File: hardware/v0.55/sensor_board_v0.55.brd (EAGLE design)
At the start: 56.4 x 56.4 mm, 58 parts, among them J3 USB-MICROB, J6 AVR_SPI_PRG_6PTH, U1 ATMEGA328P, U10 TSL2591, U2 SHT35, U3 OPA344, U5 FT231XS, U6 ADMP401, U7 RFM69HCW, U8 MCP1703CB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

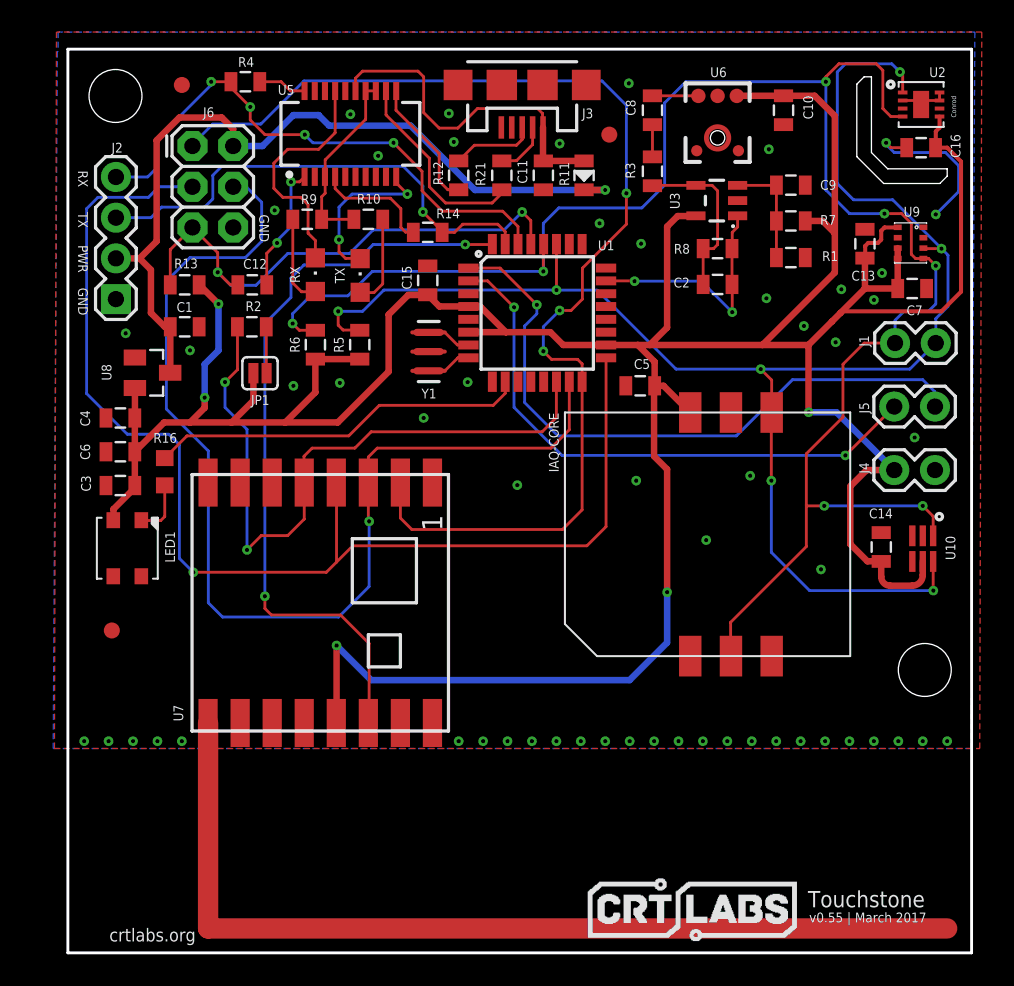
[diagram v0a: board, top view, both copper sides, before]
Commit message: v0.55 - Major design update
- Added 2x5 header for PMS7003 PM sensor
- Moved microphone+amp circuitry to accomodate for the PM sensor header
- Removed UART and software serial breakout headers
- Moved voltage regulator circuitry in space created by removing UART
header
- Moved LED in space created by moving voltage regulator
- Moved light sensor to be in line with LED
- Rerouted several traces to accomodate for new design
- Some silkscreen adjustments
- Provided some more tolerance to the mounting holes
- Moved fiducial markers
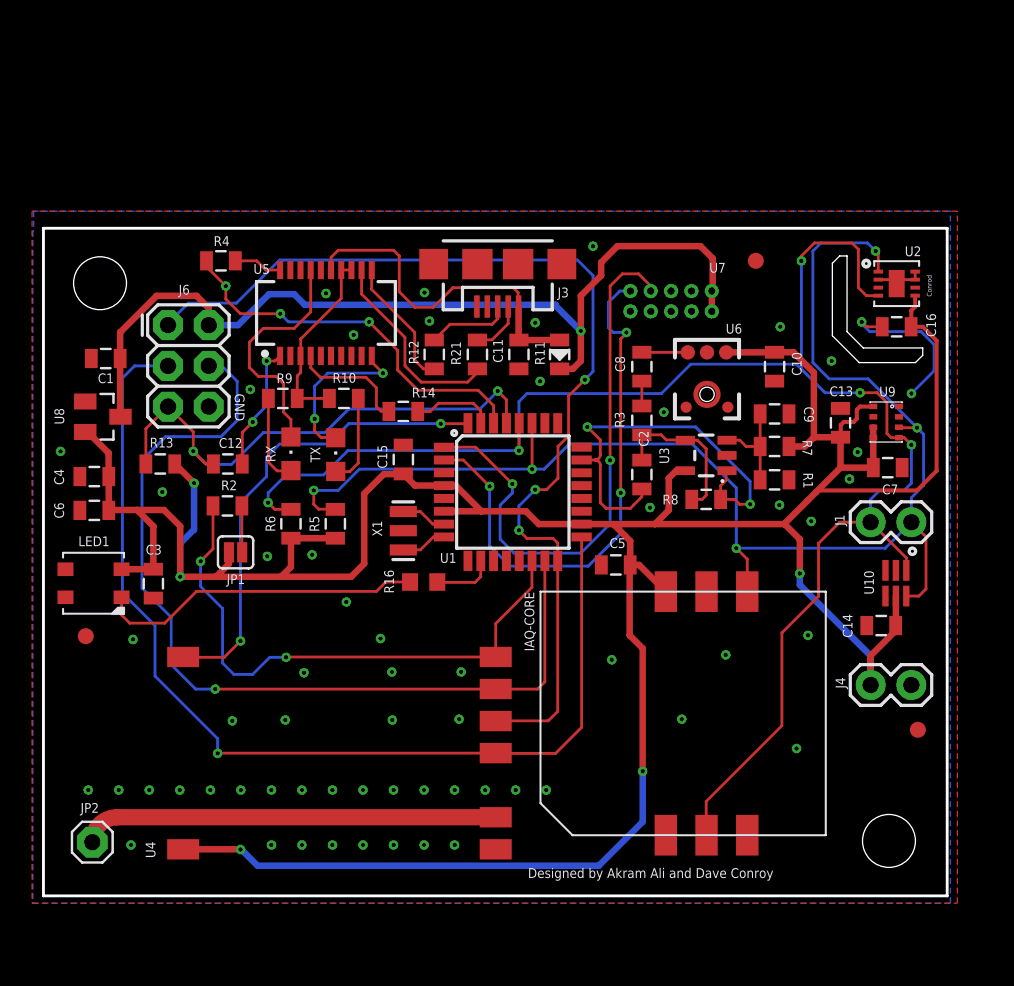
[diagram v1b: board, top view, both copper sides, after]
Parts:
- removed J2: (no value), SparkFun-Connectors:1X04
- removed J5: (no value), SparkFun-Connectors:1X02
- removed Y1: 16MHZ, SparkFun-FreqCtrl:RESONATOR-SMD
- added JP2: (no value), adafruit:1X01
- added U4: RFM69HW, RFM69 USB Gateway:LOWPOWERLAB_RFM69W-MINPADS
- added X1: 16 MHz, SparkFun:RESONATOR-SMD
- U7: value RFM69HCW -> PMS7003; device SparkFun-RF:RFM69HCW-XXXS2 -> Amphenol:RECEPTACLE_1.27MM
- moved U$2 50.7 mm to (55.6, 16.0)
- moved U7 36.7 mm to (46.6, 47.2), flipped to the bottom
- moved U$1 34.9 mm to (3.66, 21.8)
- moved R16 17.6 mm to (24.7, 25.2), turned to 0 degrees
- moved C8 16.0 mm to (38.4, 38.6)
- moved U6 16.0 mm to (42.4, 36.9)
- moved C10 16.0 mm to (46.6, 38.6)
- moved U3 15.9 mm to (42.4, 33.1)
- moved R8 15.7 mm to (42.4, 30.3)
- moved R3 15.6 mm to (38.4, 35.3)
- moved C9 14.3 mm to (46.6, 35.7)
- moved R7 14.1 mm to (46.6, 33.6)
- moved R1 13.9 mm to (46.6, 31.5)
- moved J4 13.5 mm to (55.2, 18.7)
- moved C2 12.8 mm to (38.4, 31.9), turned to 270 degrees
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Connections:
- removed net ANA: U7.9
- new net ANT: JP2.1, U4.ANA
- net D2: now also U4.DIO0; no longer U7.14
- net D3: now also U7.7; no longer J5.2
- net D4: now also U7.9; no longer J5.1
- net GND: now also U4.GND, U7.3, U7.4, X1.2; no longer J2.1, U7.1, U7.10, U7.8, Y1.2
- net MISO: now also U4.MISO; no longer U7.2
- net MOSI: now also U4.MOSI; no longer U7.3
- net N$4: now also X1.3; no longer Y1.3
- net N$5: now also X1.1; no longer Y1.1
- net PWR: now also U7.1, U7.2; no longer J2.2
- net RX: no longer J2.4
- net SCK: now also U4.SCK; no longer U7.4
- net SS: now also U4.NSS; no longer U7.5
- net TX: no longer J2.3
- net VCC: now also U4.VDD; no longer U7.13
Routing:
- net ANA: track 58.9 -> 0.00 mm
- net ANT: track 0.00 -> 25.8 mm
- net TX: track 30.4 -> 5.18 mm, vias 1 -> 0
- net VCC: track 227.2 -> 206.4 mm
- net D6: track 23.6 -> 3.86 mm
- net D2: track 47.1 -> 29.6 mm
- net N$7: track 3.52 -> 20.4 mm
- net SCK: track 76.6 -> 64.3 mm
- net SDA: track 99.0 -> 86.9 mm, vias 7 -> 5
- net A0: track 14.8 -> 26.8 mm
- net MOSI: track 68.3 -> 56.8 mm
- net SCL: track 114.0 -> 103.0 mm, vias 7 -> 5
- net RX: track 35.0 -> 24.2 mm, vias 4 -> 3
- net MISO: track 73.6 -> 64.3 mm
- net SS: track 42.1 -> 35.4 mm
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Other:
- board size 56.4 x 56.4 mm -> 56.4 x 41.7 mm
- board text added: "U7"
- board text added: "v0.55 | April 2017"
- board text removed: "PWR"
- board text removed: "RX"
- board text removed: "TX"
- board text removed: "v0.55 | March 2017"

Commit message: v0.55 - major update 2
- Added 915MHz chip antenna (JT 0868AT43A0020E) using ref. designs from:
https://www.johansontechnology.com/datasheets/antennas/0868AT43A0020.pdf
and http://www.ti.com/lit/an/swra160b/swra160b.pdf
- Replaced RFM69HW with RFM69HCW to accomodate for space for chip
antenna
- Rerouted traces to accomodate for new parts
- Adjusted silkscreen
- Minor adjustments to board dimensions (slight increase along Y axis)
- Other minor adjustments to traces, vias, silkscreen
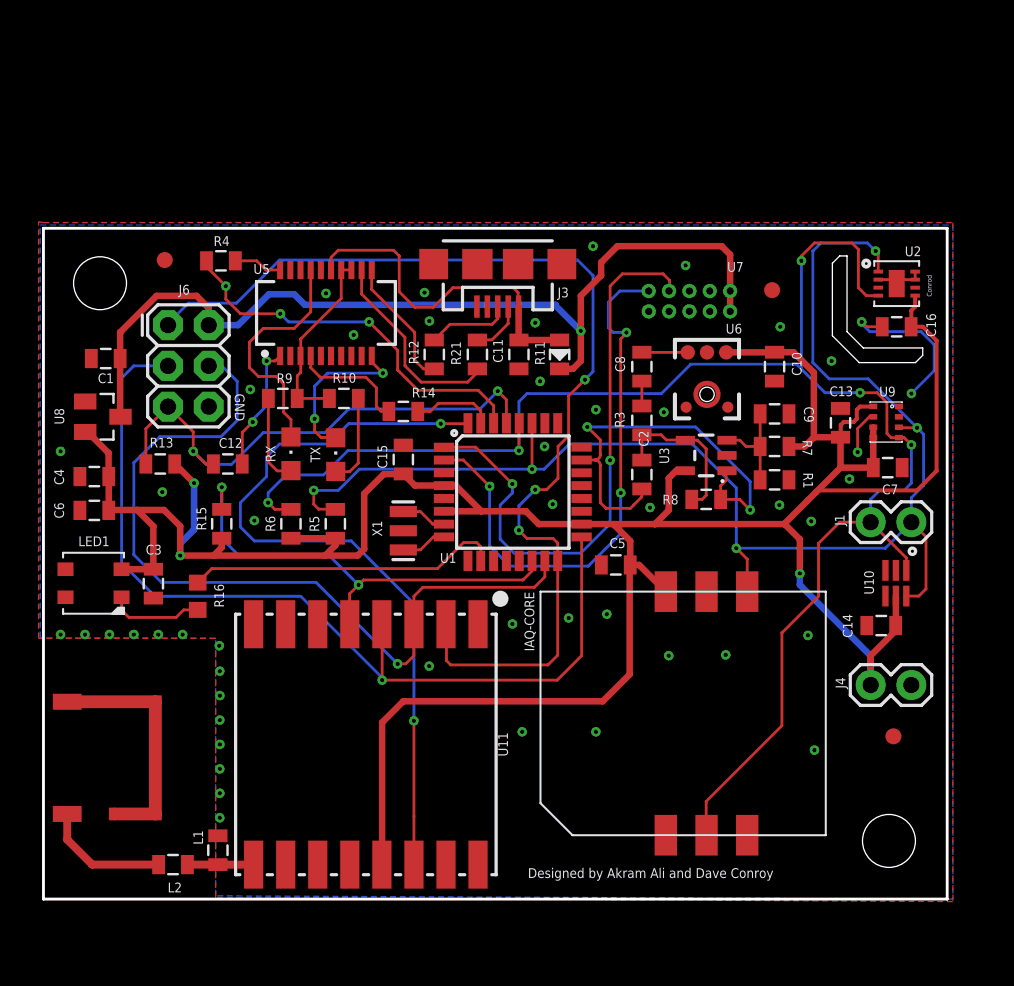
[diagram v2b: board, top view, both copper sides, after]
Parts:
- removed JP1: JUMPER-PAD-2-NC_BY_PASTEFULL-BOX-SILK, SparkFun-Passives:PAD-JUMPER-2-NC_BY_PASTE_YES_SILK_FULL_BOX
- removed JP2: (no value), adafruit:1X01
- removed R2: 10K, SparkFun-Passives:0805
- removed U4: RFM69HW, RFM69 USB Gateway:LOWPOWERLAB_RFM69W-MINPADS
- added L1: 12nH, SparkFun-Passives:0805
- added L2: 1.8nH, SparkFun-Passives:0805
- added R15: 10K, SparkFun-Passives:0805
- added U$4: 0868AT43A0020E, johanson-technology:SMD_CHIP
- added U11: 915MHz, SparkFun-RF:RFM69HCW-XXXS2
- moved U$1 24.0 mm to (8.59, 45.3)
- moved R16 14.1 mm to (10.6, 24.3), turned to 90 degrees
- moved U$3 2.09 mm to (46.5, 43.4)
- moved U$2 1.58 mm to (54.1, 15.5)
- moved U7 1.14 mm to (47.7, 47.2)
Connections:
- new net FEED: L1.1, L2.1, U11.9
- net ANT: now also U$4.P$2; no longer JP2.1, U4.ANA
- net D2: now also U11.14; no longer U4.DIO0
- net GND: now also L1.2, U11.1, U11.10, U11.8; no longer U4.GND
- net MISO: now also U11.2; no longer U4.MISO
- net MOSI: now also U11.3; no longer U4.MOSI
- net N$1: now also L2.2, U$4.P$1; no longer JP1.1, R2.2
- net SCK: now also U11.4; no longer U4.SCK
- net SS: now also R15.1, U11.5; no longer R2.1, U4.NSS
- net VCC: now also R15.2, U11.13; no longer JP1.2, U4.VDD
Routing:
- net VCC: track 206.4 -> 186.7 mm, vias 5 -> 3
- net D2: track 29.6 -> 47.6 mm
- net D6: track 3.86 -> 19.7 mm
- net N$7: track 20.4 -> 5.94 mm
- net ANT: track 25.8 -> 15.0 mm
- net SS: track 35.4 -> 28.8 mm
- net SCK: track 64.3 -> 58.1 mm
- net N$1: track 2.90 -> 7.95 mm
- net MOSI: track 56.8 -> 51.8 mm
- net FEED: track 0.00 -> 4.13 mm
- net GND: track 13.2 -> 16.0 mm, vias 61 -> 49
- net MISO: track 64.3 -> 66.2 mm
- net D3: track 35.3 -> 36.7 mm
- net PWR: track 57.4 -> 58.6 mm
- net D4: track 34.0 -> 35.1 mm
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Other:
- board size 56.4 x 41.7 mm -> 56.4 x 41.9 mm

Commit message: Shifted IAQ core lower
So it aligns with the Radio a bit more. Rerouted some traces and
rearranged the decoupling cap
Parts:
- moved C5 4.02 mm to (40.7, 26.1), turned to 0 degrees
- moved IAQ-CORE 1.78 mm to (32.0, 7.59)
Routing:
- net VCC: track 186.7 -> 190.0 mm
- net SCL: track 103.0 -> 104.8 mm
- net SDA: track 86.9 -> 88.6 mm
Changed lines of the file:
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@@
 <setting verticaltext="up"/>
 </settings>
-<grid distance="10" unitdist="mil" unit="mil" style="lines" multiple="1" display="yes" altdistance="1" altunitdist="mil" altunit="mm"/>
+<grid distance="5" unitdist="mil" unit="mil" style="lines" multiple="1" display="yes" altdistance="1" altunitdist="mil" altunit="mm"/>
 <layers>
 <layer number="1" name="Top" color="4" fill="1" visible="yes" active="yes"/>
@@
 <plain>
 <text x="36.6268" y="10.9728" size="1.016" layer="122" font="vector" ratio="16" rot="MR0" align="center-left">Touchstone</text>
-<text x="31.242" y="6.7056" size="0.6096" layer="121" font="vector">Designed by Akram Ali and Dave Conroy</text>
+<text x="50.546" y="6.7056" size="0.6096" layer="122" font="vector" rot="MR0">Designed by Akram Ali and Dave Conroy</text>
 <text x="36.5506" y="9.525" size="0.6096" layer="122" font="vector" rot="MR0">v0.55 | April 2017</text>
-<text x="43.3324" y="7.62" size="0.8128" layer="122" font="vector" ratio="12" rot="MR180">crtlabs.org</text>
+<text x="36.5506" y="9.144" size="0.8128" layer="122" font="vector" ratio="12" rot="MR180" align="bottom-right">crtlabs.org</text>
 <rectangle x1="43.4086" y1="8.3566" x2="43.815" y2="8.4074" layer="122" rot="R180"/>
 <rectangle x1="43.3578" y1="8.4074" x2="43.9166" y2="8.4582" layer="122" rot="R180"/>
@@
 </autorouter>
 <elements>
-<element name="IAQ-CORE" library="IAQ-CORE" package="IAQ-CORE" value="IAQ-CORE" x="32.0294" y="9.3726" smashed="yes" rot="R90">
-<attribute name="MF" value="" x="32.0294" y="9.3726" size="1.778" layer="27" rot="R90" display="off"/>
-<attribute name="MPN" value="IAQ-CORE C" x="32.0294" y="9.3726" size="1.778" layer="27" rot="R90" display="off"/>
-<attribute name="NAME" x="31.0322" y="24.5618" size="0.6096" layer="121" font="vector" rot="R270"/>
-<attribute name="OC_NEWARK" value="82Y5455" x="32.0294" y="9.3726" size="1.778" layer="27" rot="R90" display="off"/>
+<element name="IAQ-CORE" library="IAQ-CORE" package="IAQ-CORE" value="IAQ-CORE" x="32.0294" y="7.5946" smashed="yes" rot="R90">
+<attribute name="MF" value="" x="32.0294" y="7.5946" size="1.778" layer="27" rot="R90" display="off"/>
+<attribute name="MPN" value="IAQ-CORE C" x="32.0294" y="7.5946" size="1.778" layer="27" rot="R90" display="off"/>
+<attribute name="NAME" x="31.0322" y="22.7838" size="0.6096" layer="121" font="vector" rot="R270"/>
+<attribute name="OC_NEWARK" value="82Y5455" x="32.0294" y="7.5946" size="1.778" layer="27" rot="R90" display="off"/>
 </element>
 <element name="U1" library="SparkFun-DigitalIC" package="TQFP32-08" value="ATMEGA328P" x="30.3022" y="30.7848" smashed="yes">
@@
 <attribute name="NAME" x="15.4813" y="28.8036" size="0.6096" layer="121" font="vector" rot="R90" align="bottom-center"/>
 </element>
-<element name="C5" library="SparkFun-Passives" package="0805" value="0.1uF" x="36.7284" y="26.2382" smashed="yes" rot="R180">
-<attribute name="MPN" value="CC0805KRX7R9BB104" x="36.7284" y="26.2382" size="1.778" layer="27" rot="R180" display="off"/>
-<attribute name="NAME" x="37.338" y="27.9019" size="0.6096" layer="121" font="vector" rot="R180"/>
+<element name="C5" library="SparkFun-Passives" package="0805" value="0.1uF" x="40.7416" y="26.0858" smashed="yes">
+<attribute name="MPN" value="CC0805KRX7R9BB104" x="40.7416" y="26.0858" size="1.778" layer="27" display="off"/>
+<attribute name="NAME" x="40.259" y="27.2161" size="0.6096" layer="121" font="vector"/>
 </element>
 <element name="U8" library="linear" package="SOT23" value="MCP1703CB" x="4.7244" y="35.4838" smashed="yes" rot="R270">
@@
 <via x="18.6436" y="43.18" extent="1-16" drill="0.254" diameter="0.127"/>
 <via x="50.1904" y="38.9636" extent="1-16" drill="0.254" diameter="0.127"/>
-<via x="38.862" y="29.8196" extent="1-16" drill="0.254" diameter="0.127"/>
+<via x="38.735" y="29.6926" extent="1-16" drill="0.254" diameter="0.127"/>
 <via x="48.9204" y="28.956" extent="1-16" drill="0.254" diameter="0.127"/>
 <via x="46.9392" y="29.972" extent="1-16" drill="0.254" diameter="0.127"/>
@@
 <contactref element="C13" pad="1"/>
 <contactref element="U9" pad="5"/>
-<wire x1="34.5948" y1="28.7848" x2="36.576" y2="28.7848" width="0.4064" layer="1"/>
 <wire x1="26.0096" y1="29.5848" x2="28.3464" y2="29.5848" width="0.4064" layer="1"/>
 <wire x1="28.3464" y1="29.5848" x2="31.1212" y2="29.5848" width="0.4064" layer="1"/>
@@
 <wire x1="26.0096" y1="31.1848" x2="26.7464" y2="31.1848" width="0.4064" layer="1"/>
 <wire x1="26.7464" y1="31.1848" x2="28.3464" y2="29.5848" width="0.4064" layer="1"/>
-<wire x1="39.1668" y1="28.7848" x2="36.576" y2="28.7848" width="0.4064" layer="1"/>
+<wire x1="36.576" y1="28.7848" x2="39.1668" y2="28.7848" width="0.4064" layer="1"/>
+<wire x1="36.576" y1="28.7848" x2="34.5948" y2="28.7848" width="0.4064" layer="1"/>
 <wire x1="39.1668" y1="28.7848" x2="47.2252" y2="28.7848" width="0.4064" layer="1"/>
 <wire x1="50.7492" y1="32.3088" x2="52.7956" y2="32.3088" width="0.4064" layer="1"/>
@@
 <contactref element="LED1" pad="2"/>
 <contactref element="J4" pad="2"/>
-<wire x1="37.6284" y1="26.2382" x2="38.1838" y2="26.2382" width="0.4064" layer="1"/>
-<wire x1="38.1838" y1="26.2382" x2="39.8494" y2="24.5726" width="0.4064" layer="1"/>
-<wire x1="37.6284" y1="26.2382" x2="37.592" y2="26.2018" width="0.4064" layer="1"/>
-<wire x1="37.6284" y1="26.2382" x2="37.6284" y2="27.7324" width="0.4064" layer="1"/>
-<wire x1="37.6284" y1="27.7324" x2="36.576" y2="28.7848" width="0.4064" layer="1"/>
 <contactref element="U2" pad="5"/>
 <contactref element="C16" pad="1"/>
@@
 <wire x1="55.5244" y1="30.8864" x2="49.3268" y2="30.8864" width="0.254" layer="1"/>
 <wire x1="49.3268" y1="30.8864" x2="49.2252" y2="30.7848" width="0.254" layer="1"/>
-<wire x1="41.0671" y1="32.1208" x2="40.5028" y2="32.1208" width="0.4064" layer="1"/>
-<wire x1="40.5028" y1="32.1208" x2="40.0304" y2="31.6484" width="0.4064" layer="1"/>
-<wire x1="40.0304" y1="31.6484" x2="40.0304" y2="29.6484" width="0.4064" layer="1"/>
-<wire x1="40.0304" y1="29.6484" x2="39.1668" y2="28.7848" width="0.4064" layer="1"/>
+<wire x1="40.5028" y1="32.1208" x2="41.0671" y2="32.1208" width="0.4064" layer="1"/>
 <wire x1="43.618" y1="39.5008" x2="46.6272" y2="39.5008" width="0.4064" layer="1"/>
 <wire x1="46.6272" y1="39.5008" x2="46.6344" y2="39.508" width="0.4064" layer="1"/>
@@
 <wire x1="23.4696" y1="17.7292" x2="35.9156" y2="17.7292" width="0.4064" layer="1"/>
 <wire x1="35.9156" y1="17.7292" x2="37.592" y2="19.4056" width="0.4064" layer="1"/>
-<wire x1="37.592" y1="19.4056" x2="37.592" y2="26.2018" width="0.4064" layer="1"/>
-<wire x1="37.592" y1="26.2018" x2="37.6284" y2="26.2382" width="0.4064" layer="1"/>
 <wire x1="22.1488" y1="7.5528" x2="22.1488" y2="16.4084" width="0.4064" layer="1"/>
+<wire x1="37.592" y1="27.7688" x2="36.576" y2="28.7848" width="0.4064" layer="1"/>
+<wire x1="37.592" y1="19.4056" x2="37.592" y2="27.7688" width="0.4064" layer="1"/>
+<wire x1="39.8494" y1="26.078" x2="39.8416" y2="26.0858" width="0.4064" layer="1"/>
+<wire x1="39.8494" y1="22.7946" x2="39.8494" y2="26.078" width="0.4064" layer="1"/>
+<wire x1="39.8416" y1="26.0858" x2="39.8416" y2="28.11" width="0.4064" layer="1"/>
+<wire x1="39.8416" y1="28.11" x2="39.1668" y2="28.7848" width="0.4064" layer="1"/>
+<wire x1="39.1668" y1="28.7848" x2="39.1988" y2="28.7848" width="0.4064" layer="1"/>
+<wire x1="39.1988" y1="28.7848" x2="39.878" y2="29.464" width="0.4064" layer="1"/>
+<wire x1="39.878" y1="29.464" x2="39.878" y2="31.496" width="0.4064" layer="1"/>
+<wire x1="39.878" y1="31.496" x2="40.5028" y2="32.1208" width="0.4064" layer="1"/>
 </signal>
 <signal name="SCL">
@@
 <wire x1="52.6288" y1="28.9052" x2="50.6984" y2="28.9052" width="0.1778" layer="1"/>
 <wire x1="50.6984" y1="28.9052" x2="49.3776" y2="27.5844" width="0.1778" layer="1"/>
-<wire x1="47.0916" y1="21.9964" x2="47.0916" y2="16.2052" width="0.1778" layer="1"/>
-<wire x1="47.0916" y1="16.2052" x2="42.3672" y2="11.4808" width="0.1778" layer="1"/>
-<wire x1="42.3672" y1="11.4808" x2="42.3672" y2="9.3948" width="0.1778" layer="1"/>
-<wire x1="42.3672" y1="9.3948" x2="42.3894" y2="9.3726" width="0.1778" layer="1"/>
+<wire x1="47.0916" y1="21.9964" x2="47.0916" y2="16.256" width="0.1778" layer="1"/>
+<wire x1="47.0916" y1="16.256" x2="47.0916" y2="16.2052" width="0.1778" layer="1"/>
 <wire x1="51.8668" y1="43.5356" x2="51.8668" y2="45.9232" width="0.1778" layer="1"/>
 <wire x1="51.8668" y1="45.9232" x2="51.4604" y2="46.3296" width="0.1778" layer="1"/>
@@
 <wire x1="54.8536" y1="25.8952" x2="54.8536" y2="26.6804" width="0.1778" layer="1"/>
 <wire x1="54.8536" y1="26.6804" x2="52.6288" y2="28.9052" width="0.1778" layer="1"/>
+<wire x1="42.3894" y1="11.4586" x2="42.3894" y2="7.5946" width="0.1778" layer="1"/>
+<wire x1="47.0916" y1="16.256" x2="47.0916" y2="16.1608" width="0.1778" layer="1"/>
+<wire x1="47.0916" y1="16.1608" x2="42.3894" y2="11.4586" width="0.1778" layer="1"/>
 </signal>
 <signal name="SDA">
@@
 <wire x1="20.7326" y1="32.2134" x2="31.5022" y2="32.2134" width="0.1778" layer="16"/>
 <wire x1="20.7326" y1="32.2134" x2="19.4056" y2="30.8864" width="0.1778" layer="16"/>
-<wire x1="44.9294" y1="24.5726" x2="44.9294" y2="26.597" width="0.1778" layer="1"/>
 <wire x1="44.9294" y1="26.597" x2="44.2468" y2="27.2796" width="0.1778" layer="1"/>
 <wire x1="55.1688" y1="28.9052" x2="53.5432" y2="27.2796" width="0.1778" layer="16"/>
@@
 <wire x1="56.0832" y1="27.9908" x2="55.1688" y2="28.9052" width="0.1778" layer="1"/>
 <wire x1="54.8536" y1="24.2952" x2="55.6388" y2="24.2952" width="0.1778" layer="1"/>
+<wire x1="44.9294" y1="22.7946" x2="44.9294" y2="26.597" width="0.1778" layer="1"/>
 </signal>
 <signal name="N$4">
